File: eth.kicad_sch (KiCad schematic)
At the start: 43 parts, among them J6 RJ45_Abracon_ARJP11A-MASA-B-A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, U26 LAN8742A, U27 USBLC6-4SC6, Y2 25MHz

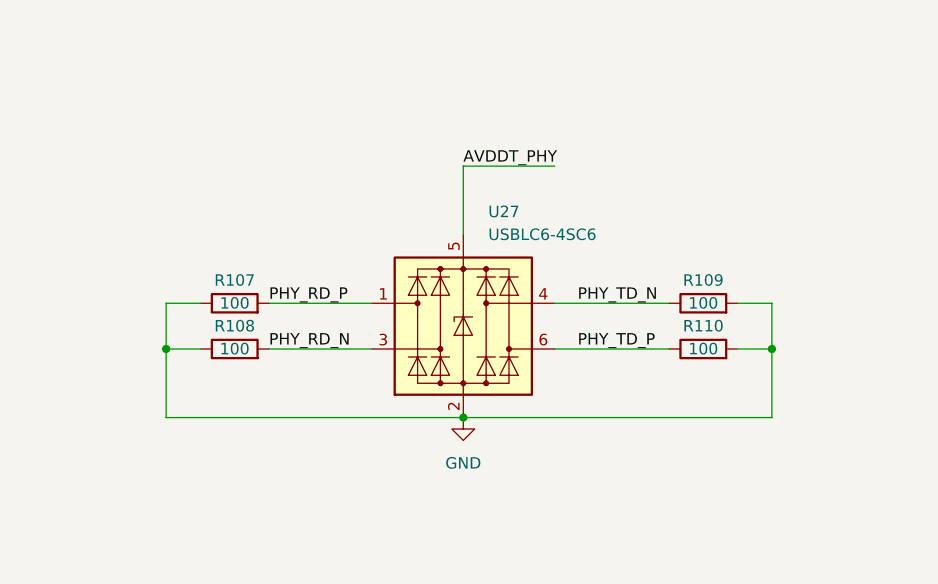
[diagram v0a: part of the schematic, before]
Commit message: sch: correct ethernet phy sigs connections to ESD - Pull up eth signals with 100R instead of pull down
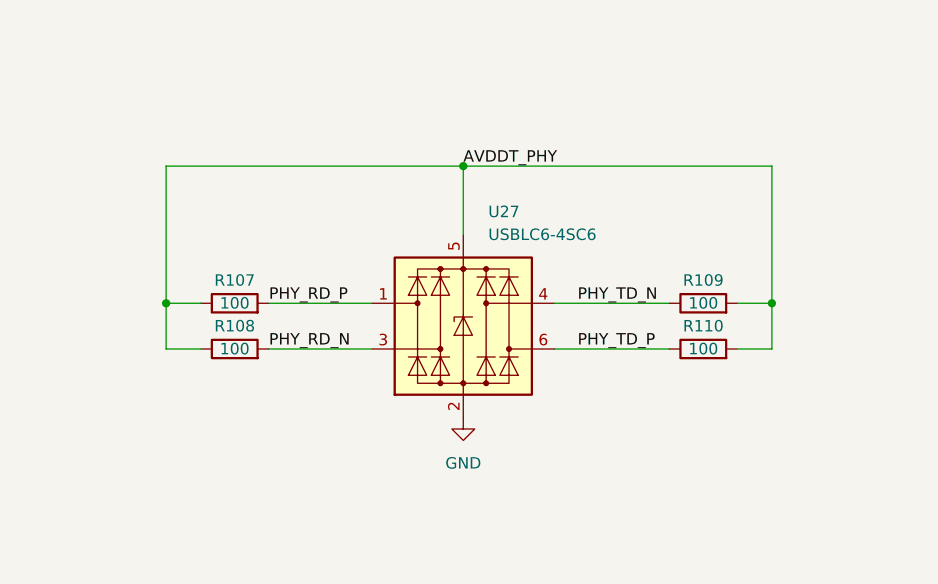
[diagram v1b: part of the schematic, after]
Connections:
- net AVDDT_PHY: now also R107.1, R108.1, R109.2, R110.2
- net GND: no longer R107.1, R108.1, R109.2, R110.2
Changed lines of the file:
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@@
   (junction (at 334.01 125.73) (diameter 0) (color 0 0 0 0)
   )
+  (junction (at 157.48 76.2) (diameter 0) (color 0 0 0 0)
+  )
   (junction (at 109.22 168.91) (diameter 0) (color 0 0 0 0)
   )
@@
   (junction (at 300.99 201.93) (diameter 0) (color 0 0 0 0)
   )
-  (junction (at 191.77 96.52) (diameter 0) (color 0 0 0 0)
-  )
   (junction (at 135.89 147.32) (diameter 0) (color 0 0 0 0)
   )
+  (junction (at 191.77 91.44) (diameter 0) (color 0 0 0 0)
+  )
   (junction (at 300.99 184.15) (diameter 0) (color 0 0 0 0)
   )
-  (junction (at 124.46 96.52) (diameter 0) (color 0 0 0 0)
-  )
   (junction (at 236.22 184.15) (diameter 0) (color 0 0 0 0)
   )
@@
   (junction (at 127 208.28) (diameter 0) (color 0 0 0 0)
   )
-  (junction (at 157.48 104.14) (diameter 0) (color 0 0 0 0)
-  )
   (junction (at 261.62 201.93) (diameter 0) (color 0 0 0 0)
   )
@@
   (junction (at 223.52 189.23) (diameter 0) (color 0 0 0 0)
   )
+  (junction (at 124.46 91.44) (diameter 0) (color 0 0 0 0)
+  )
   (junction (at 118.11 147.32) (diameter 0) (color 0 0 0 0)
   )
@@
     (stroke (width 0) (type default))
   )
+  (wire (pts (xy 124.46 76.2) (xy 157.48 76.2))
+    (stroke (width 0) (type default))
+  )
   (wire (pts (xy 236.22 199.39) (xy 236.22 201.93))
     (stroke (width 0) (type default))
@@
     (stroke (width 0) (type default))
   )
+  (wire (pts (xy 191.77 91.44) (xy 191.77 76.2))
+    (stroke (width 0) (type default))
+  )
   (wire (pts (xy 193.04 166.37) (xy 209.55 166.37))
     (stroke (width 0) (type default))
@@
     (stroke (width 0) (type default))
   )
-  (wire (pts (xy 124.46 104.14) (xy 157.48 104.14))
-    (stroke (width 0) (type default))
-  )
   (wire (pts (xy 248.92 184.15) (xy 261.62 184.15))
     (stroke (width 0) (type default))
@@
     (stroke (width 0) (type default))
   )
-  (wire (pts (xy 191.77 104.14) (xy 157.48 104.14))
-    (stroke (width 0) (type default))
-  )
   (wire (pts (xy 193.04 191.77) (xy 199.39 191.77))
     (stroke (width 0) (type default))
@@
     (stroke (width 0) (type default))
   )
-  (wire (pts (xy 157.48 76.2) (xy 167.64 76.2))
+  (wire (pts (xy 157.48 76.2) (xy 191.77 76.2))
     (stroke (width 0) (type default))
   )
@@
     (stroke (width 0) (type default))
   )
-  (wire (pts (xy 124.46 96.52) (xy 124.46 104.14))
+  (wire (pts (xy 124.46 91.44) (xy 124.46 76.2))
     (stroke (width 0) (type default))
   )
@@
     (stroke (width 0) (type default))
   )
-  (wire (pts (xy 191.77 96.52) (xy 191.77 104.14))
-    (stroke (width 0) (type default))
-  )

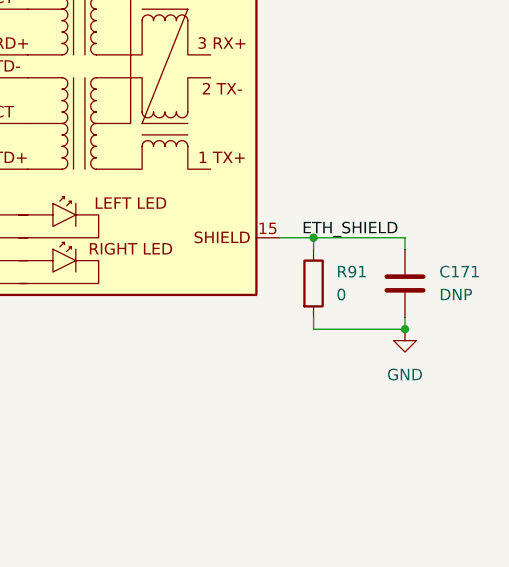
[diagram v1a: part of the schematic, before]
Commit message: sch: Set DNP for DNP components
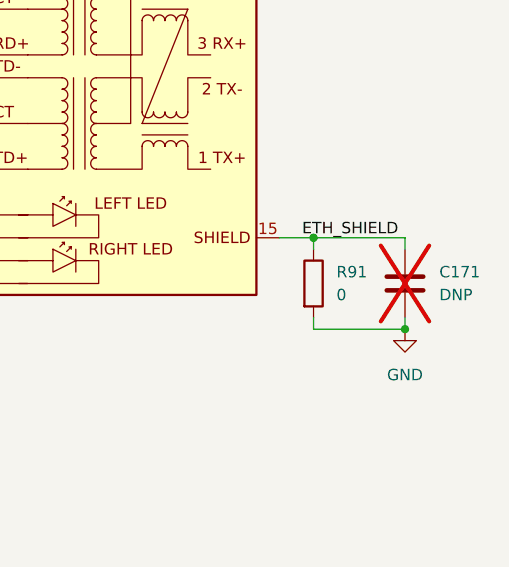
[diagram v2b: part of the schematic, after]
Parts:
- C171: now not fitted
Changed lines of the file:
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@@
   )
   (symbol (lib_id "Device:C") (at 334.01 120.65 0) (unit 1)
-    (in_bom yes) (on_board yes) (dnp no) (fields_autoplaced)
+    (in_bom yes) (on_board yes) (dnp yes) (fields_autoplaced)
     (property "Reference" "C171" (at 337.82 119.3799 0)
       (effects (font (size 1.27 1.27)) (justify left))

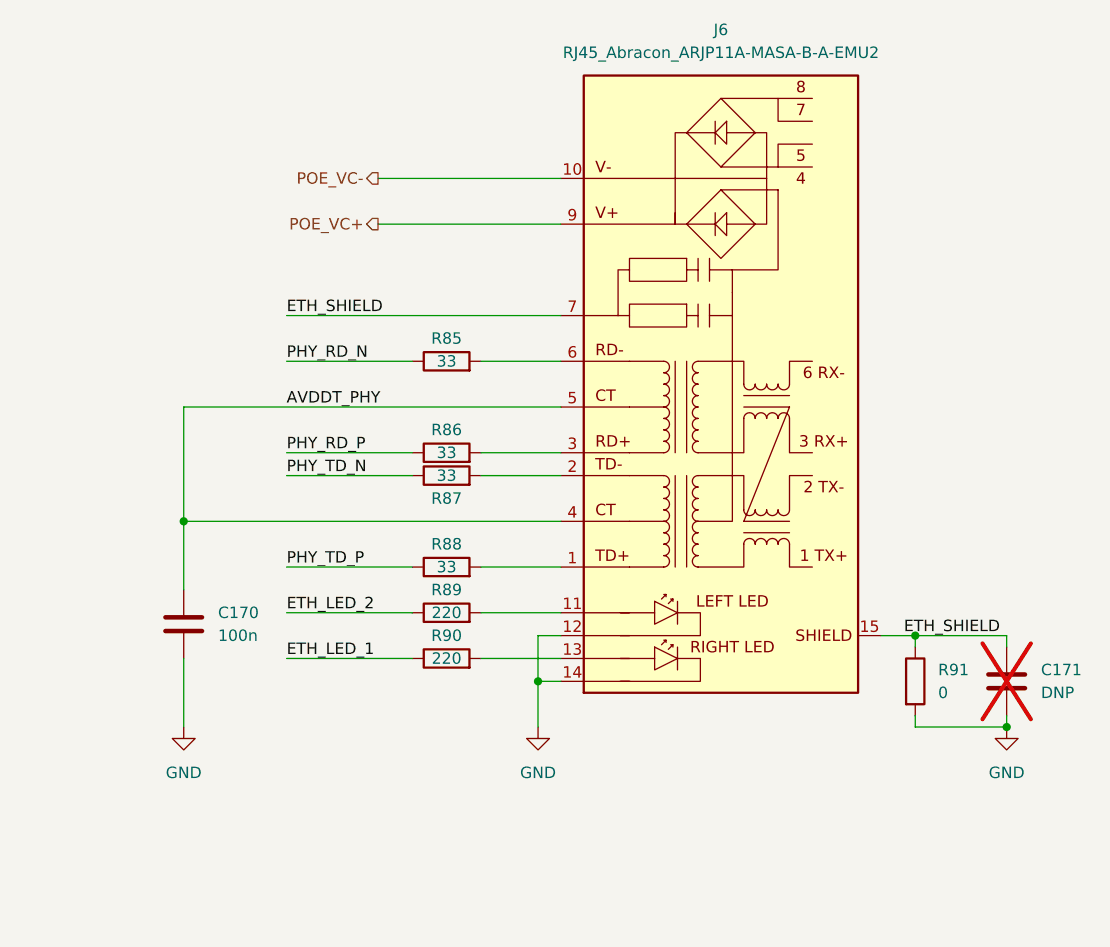
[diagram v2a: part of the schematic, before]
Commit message: sch: Change PoE RJ45 Jack and change PM1202 Symbol - Use the same PoE RJ45 as sinara-hw thermostat - Add PM1202 Power input pins (VB+, VB-) - Remove PoE softstart circuit as PM1202 has inrush current limiting - Add Pi Filter at the output of PM1202
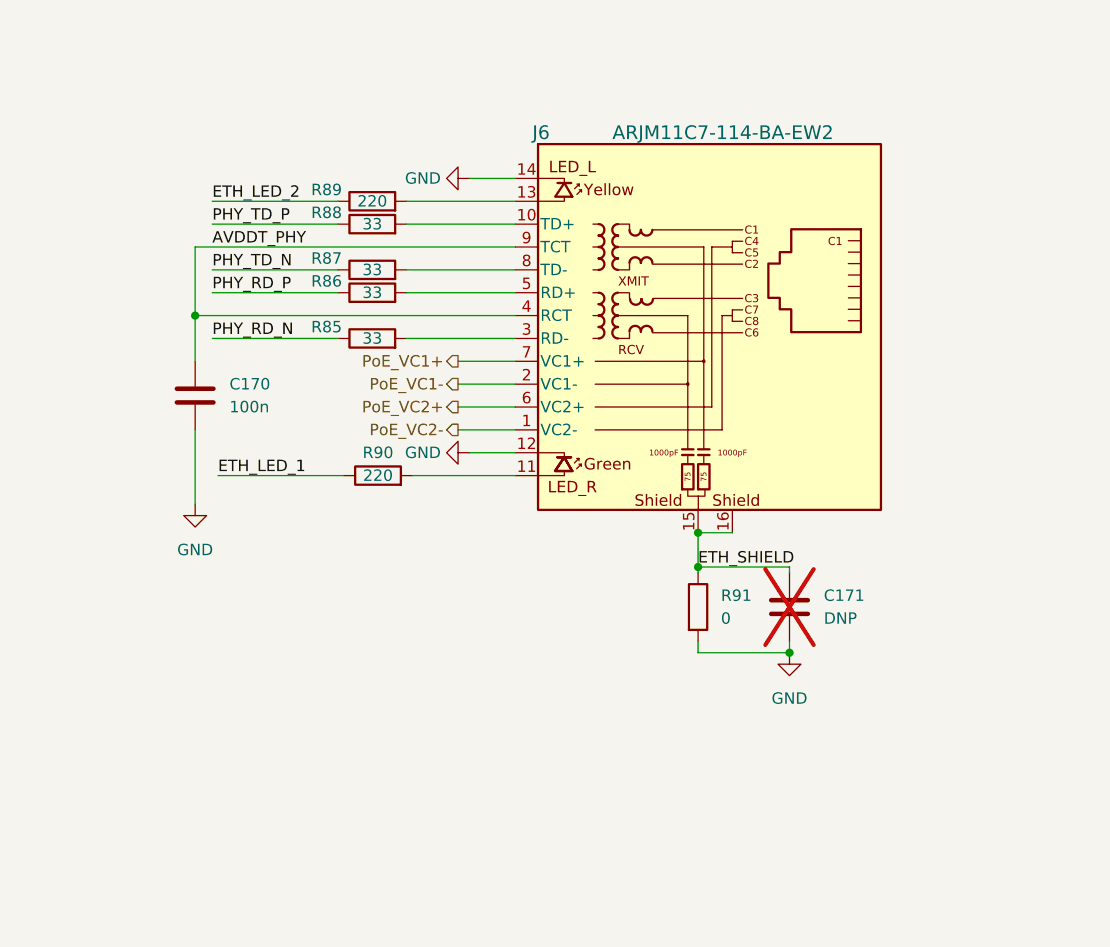
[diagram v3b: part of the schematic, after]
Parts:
- removed J6: RJ45_Abracon_ARJP11A-MASA-B-A-EMU2, Connector_RJ:RJ45_Abracon_ARJP11A-MA_Horizontal, symbol Connector:RJ45_Abracon_ARJP11A-MASA-B-A-EMU2
- added J6: ARJM11C7-114-BA-EW2, kirdy:ARJM11C7-114-BA-EW2_ABR, symbol kirdy:RJ45_ARJM11C7-114-BA-EW2
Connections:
- net AVDDT_PHY: now also J6.4 (RCT), J6.9 (TCT)
- net ETH_SHIELD: now also J6.15, J6.16
- net GND: now also J6.12, J6.14
- net at R90.2: now also J6.11
- net at R89.2: now also J6.13
- net at R85.2: now also J6.3 (RD-)
- net at R87.2: now also J6.8 (TD-)
- net at R86.2: now also J6.5 (RD+)
- net at R88.2: now also J6.10 (TD+)
- new net PoE_VC1+: J6.7 (VC1+)
- new net PoE_VC1-: J6.2 (VC1-)
- new net PoE_VC2+: J6.6 (VC2+)
- new net PoE_VC2-: J6.1 (VC2-)

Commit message: symbol: correct RJ45 VC output pin type - from power input to power output
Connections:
- net at J6.8 (TD-): now also R87.2

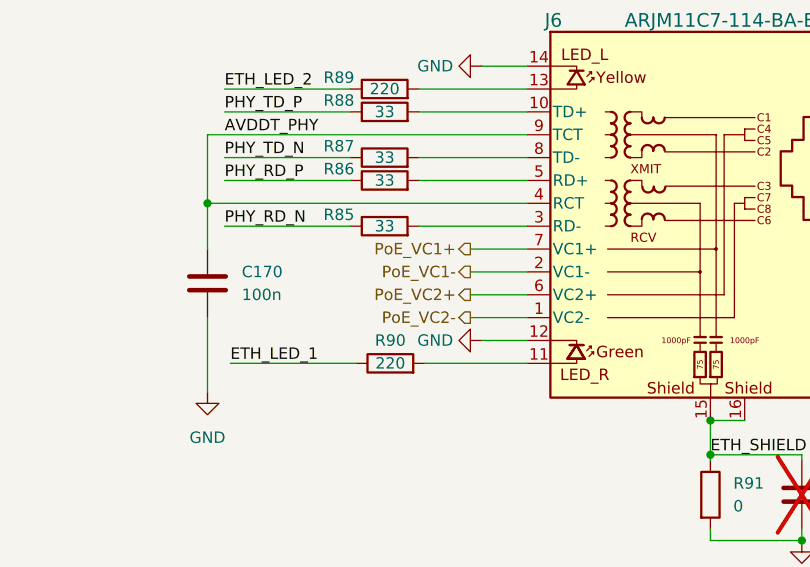
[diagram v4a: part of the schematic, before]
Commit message: sch: correct POE_VC* pins name case - PoE_VC* -> POE_VC*
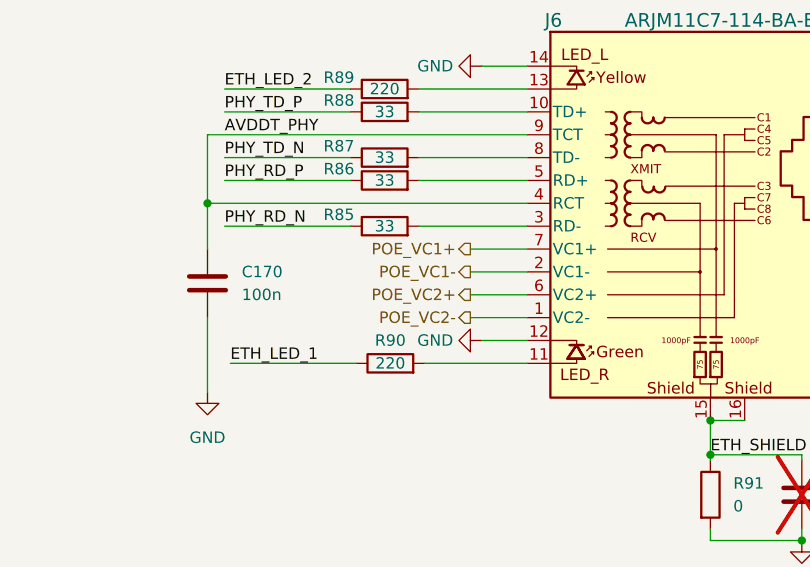
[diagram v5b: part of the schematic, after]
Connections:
- net at J6.8 (TD-): now also R87.2
- net PoE_VC1+ renamed POE_VC1+
- net PoE_VC1- renamed POE_VC1-
- net PoE_VC2+ renamed POE_VC2+
- net PoE_VC2- renamed POE_VC2-
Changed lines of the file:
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@@
     (effects (font (size 1.27 1.27)) (justify right))
   )
-  (hierarchical_label "PoE_VC1+" (shape output) (at 273.05 85.09 180) (fields_autoplaced)
+  (hierarchical_label "POE_VC1+" (shape output) (at 273.05 85.09 180) (fields_autoplaced)
     (effects (font (size 1.27 1.27)) (justify right))
   )
@@
     (effects (font (size 1.27 1.27)) (justify right))
   )
-  (hierarchical_label "PoE_VC2+" (shape output) (at 273.05 90.17 180) (fields_autoplaced)
+  (hierarchical_label "POE_VC2+" (shape output) (at 273.05 90.17 180) (fields_autoplaced)
     (effects (font (size 1.27 1.27)) (justify right))
   )
-  (hierarchical_label "PoE_VC2-" (shape output) (at 273.05 92.71 180) (fields_autoplaced)
+  (hierarchical_label "POE_VC2-" (shape output) (at 273.05 92.71 180) (fields_autoplaced)
     (effects (font (size 1.27 1.27)) (justify right))
   )
@@
     (effects (font (size 1.27 1.27)) (justify right))
   )
-  (hierarchical_label "PoE_VC1-" (shape output) (at 273.05 87.63 180) (fields_autoplaced)
+  (hierarchical_label "POE_VC1-" (shape output) (at 273.05 87.63 180) (fields_autoplaced)
     (effects (font (size 1.27 1.27)) (justify right))
   )

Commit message: sch: Update power related flags and nets symbols - Update the symbol from the kicad 7 built-in library - Remove ERC warnings
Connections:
- net at J6.8 (TD-): now also R87.2
